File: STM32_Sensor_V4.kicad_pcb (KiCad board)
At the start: 2 copper layers, 35.6 x 20.3 mm, 26 parts, among them J1 Conn Side, J2 Conn Down, J3 Conn Up, J4 Conn Prog, J5 u.FL, SW1 SW_Reset, SW2 SW_BOOT, U1 STM32F103C8Tx, U2 RFM69, U3 RFM69HW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

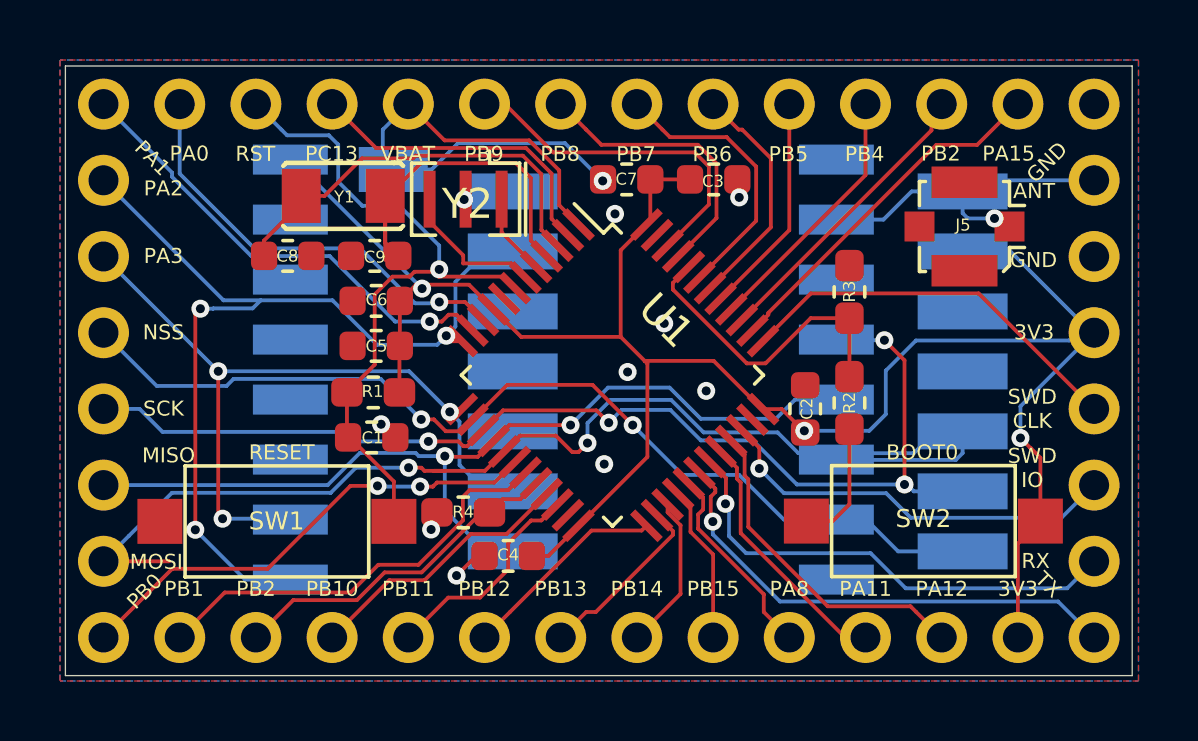
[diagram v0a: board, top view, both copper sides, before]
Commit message: Minor changes to traces
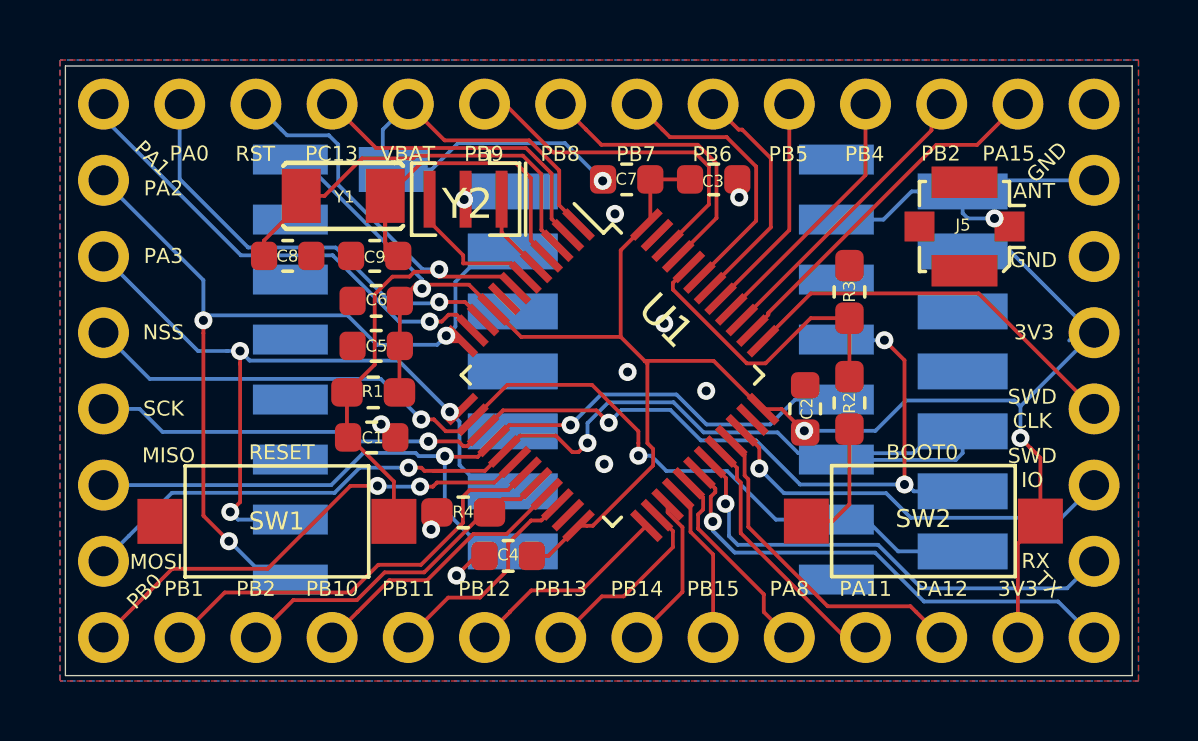
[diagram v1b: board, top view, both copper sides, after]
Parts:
- U2: value RFM69 -> RFM69CW
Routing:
- net +3V3: track 71.0 -> 68.4 mm
- net MOSI: track 39.5 -> 37.3 mm
- net PA2: track 32.1 -> 30.1 mm

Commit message: Added zones edge clearance
Added 20 mils clearance between zones and edge to conform to pcbs.io
manufacturing standards.
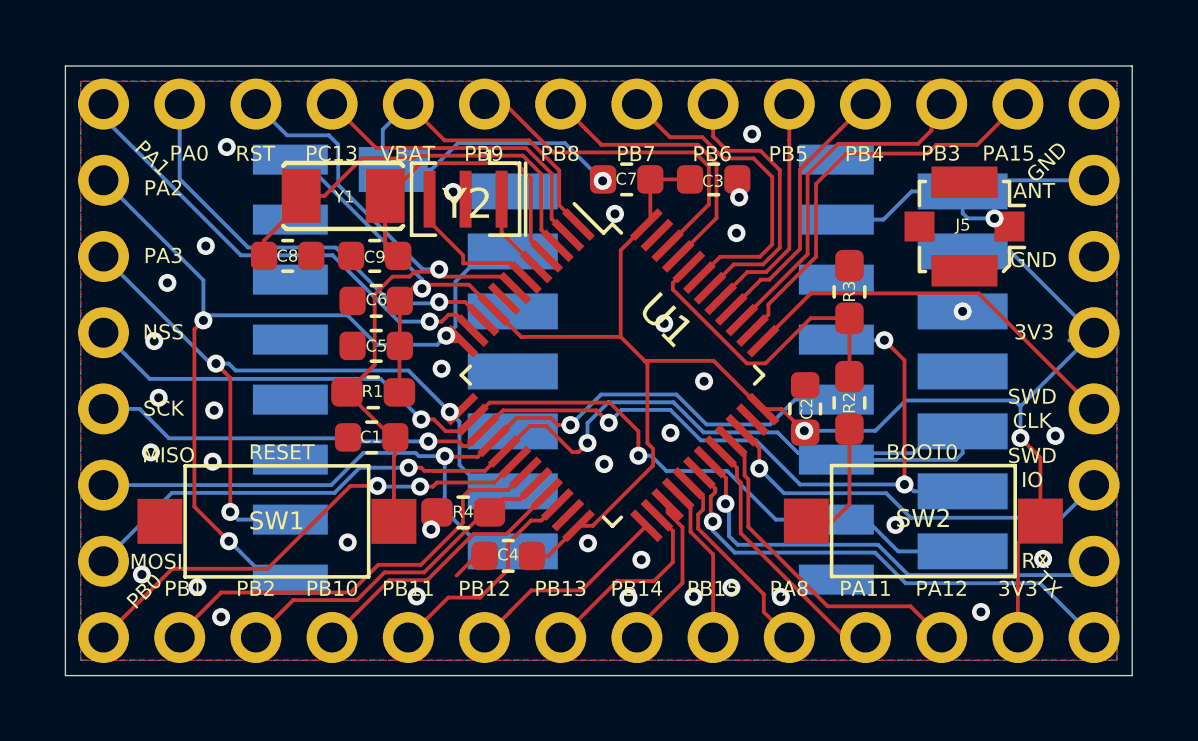
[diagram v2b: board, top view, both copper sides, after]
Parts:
- turned C1 to 180 degrees
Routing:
- net PA15: track 12.0 -> 13.6 mm
- net PB3: track 9.96 -> 11.5 mm
- net PB6: track 7.84 -> 9.24 mm
- net PB7: track 9.32 -> 10.6 mm
- net GND: track 3.31 -> 3.29 mm, vias 10 -> 35
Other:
- board text removed: "PA4"
- board text removed: "STM32 Sensor V4 by freynder"

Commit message: Added support for RFM69HCW
Previously only RFM69CW and RFM69(H)W were supported.
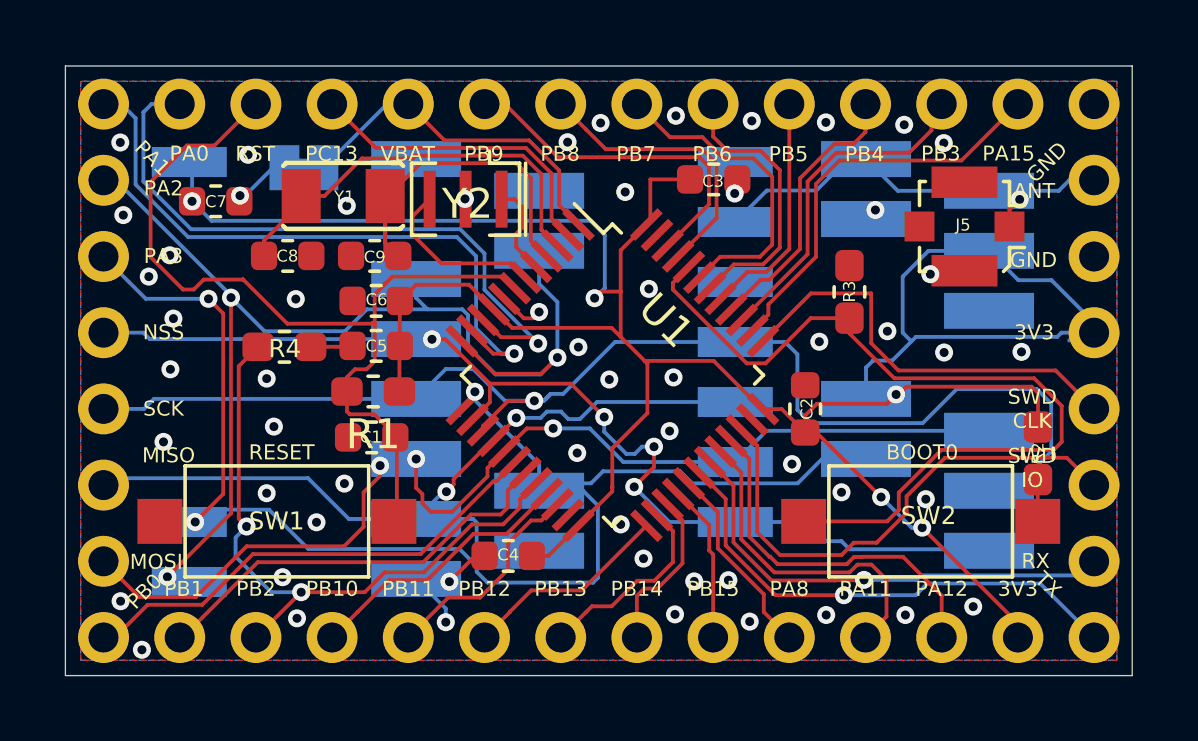
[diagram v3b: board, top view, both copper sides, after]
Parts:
- added U4: RFM69HCW, custom:RFM69HCW-XXXS2-MINPADS, B.Cu at (146.1, 100.5)
- U2: footprint RF:RFM69CW-XXXS2 -> custom:RFM69CW-XXXS2-MINPADS
- U3: footprint RF_Module:HOPERF_RFM69HW -> custom:HOPERF_RFM69HW-MINPADS
- moved C7 13.7 mm to (131.9, 94.9), turned to 0 degrees
- moved R4 8.12 mm to (134.2, 99.8), turned to 180 degrees
- moved R2 6.51 mm to (159.3, 103.3), turned to 270 degrees
- moved U3 3.37 mm to (140.1, 100.6)
- moved JP1 2.98 mm to (134.8, 93.8), turned to 180 degrees
- moved U2 0.88 mm to (150.2, 100.6)
- moved SW2 0.09 mm to (155.4, 105.6)
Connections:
- R2 pad 1: Net-(R2-Pad1) -> +3V3
- R2 pad 2: BOOT0 -> Net-(R2-Pad2)
- SW2 pad 1: Net-(R2-Pad1) -> BOOT0
- SW2 pad 2: +3V3 -> Net-(R2-Pad2)
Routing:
- net +3V3: track 68.4 -> 96.7 mm, vias 3 -> 5
- net PA3: track 25.4 -> 48.3 mm
- net BOOT0: track 10.4 -> 28.3 mm
- net PB2: track 11.5 -> 21.8 mm, vias 0 -> 2
- net PA2: track 30.3 -> 38.5 mm
- net PA0: track 14.6 -> 21.9 mm
- net RST: track 23.6 -> 30.5 mm, vias 1 -> 0
- net PA1: track 16.0 -> 21.6 mm
- net SCK: track 37.8 -> 43.2 mm, vias 4 -> 1
- net Net-(C7-Pad2): track 7.27 -> 1.87 mm
- net NSS: track 31.9 -> 36.2 mm, vias 2 -> 4
- net GND: track 3.29 -> 7.47 mm, vias 35 -> 56
- net Net-(R2-Pad1): track 4.17 -> 0.00 mm
- net ANT: track 13.0 -> 17.0 mm
- net SWDIO: track 13.8 -> 17.2 mm, vias 1 -> 0
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
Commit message: Optimize fab and silk layer
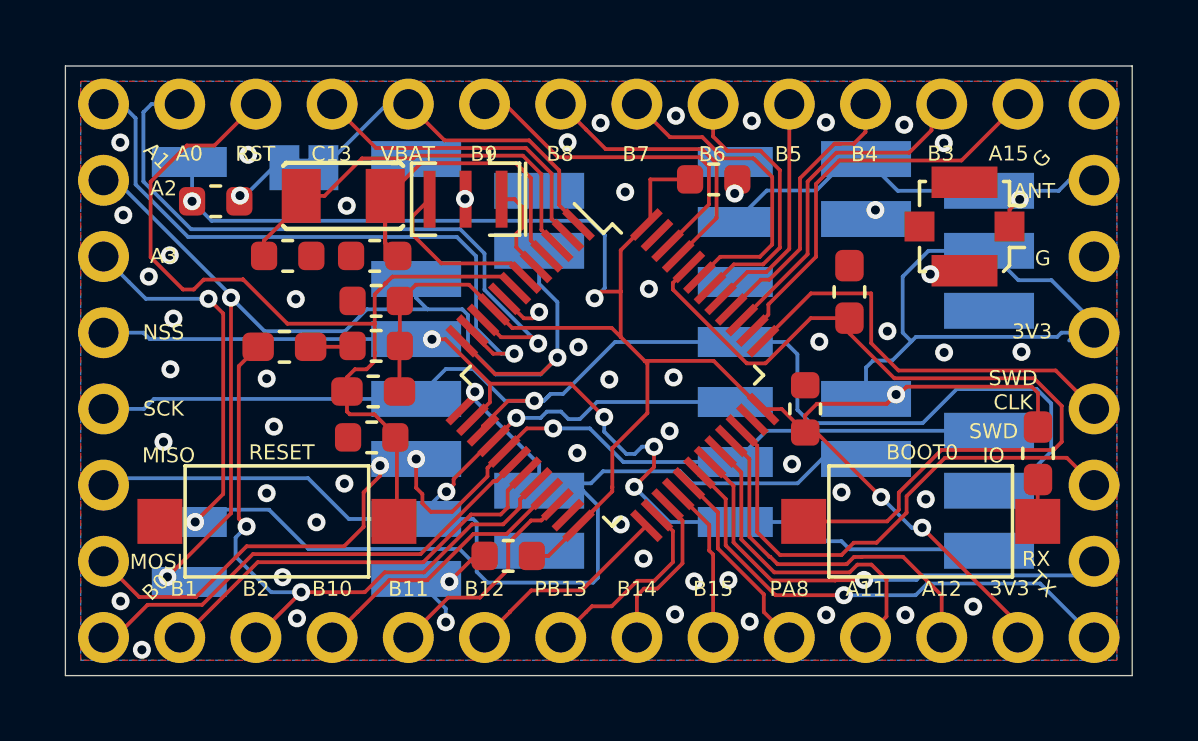
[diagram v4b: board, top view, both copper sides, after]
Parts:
- Y1: value 32768 Crystal -> 32768Mhz
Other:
- board text added: "A0"
- board text added: "A1"
- board text added: "A11"
- board text added: "A12"
- board text added: "A15"
- board text added: "A2"
- board text added: "A3"
- board text added: "A8"
- board text added: "B0"
- board text added: "B1"
- board text added: "B10"
- board text added: "B11"
- board text added: "B12"
- board text added: "B13"
- board text added: "B14"
- board text added: "B15"
- board text added: "B2"
- board text added: "B3"
- board text added: "B4"
- board text added: "B5"
- board text added: "B6"
- board text added: "B7"
- board text added: "B8"
- board text added: "B9"
- board text added: "C13"
- board text added: "G"
- board text added: "RFM69CW"
- board text added: "RFM69HCW"
- board text added: "STM32 Sensor Node V4.5 by freynder"
- board text removed: "GND"
- board text removed: "PA0"
- board text removed: "PA1"
- board text removed: "PA11"
- board text removed: "PA12"
- board text removed: "PA15"
- board text removed: "PA2"
- board text removed: "PA3"
- board text removed: "PB0"
- board text removed: "PB1"
- board text removed: "PB10"
- board text removed: "PB11"
- board text removed: "PB12"
- board text removed: "PB14"
- board text removed: "PB15"
- board text removed: "PB2"
- board text removed: "PB3"
- board text removed: "PB4"
- board text removed: "PB5"
- board text removed: "PB6"
- board text removed: "PB7"
- board text removed: "PB8"
- board text removed: "PB9"
- board text removed: "PC13"
- board text removed: "RFM69"
